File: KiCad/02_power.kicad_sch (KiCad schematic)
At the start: 51 parts, among them IC201 MCP73831T-2ACI_OT, J201 Barrel_Jack_Switch_Pin3Ring, J202 BM02B-GHS-TBT_LF__SN__N_, Q201 DMG3415U-7, U201 AMS1117-3.3, U202 TLV62569DBV

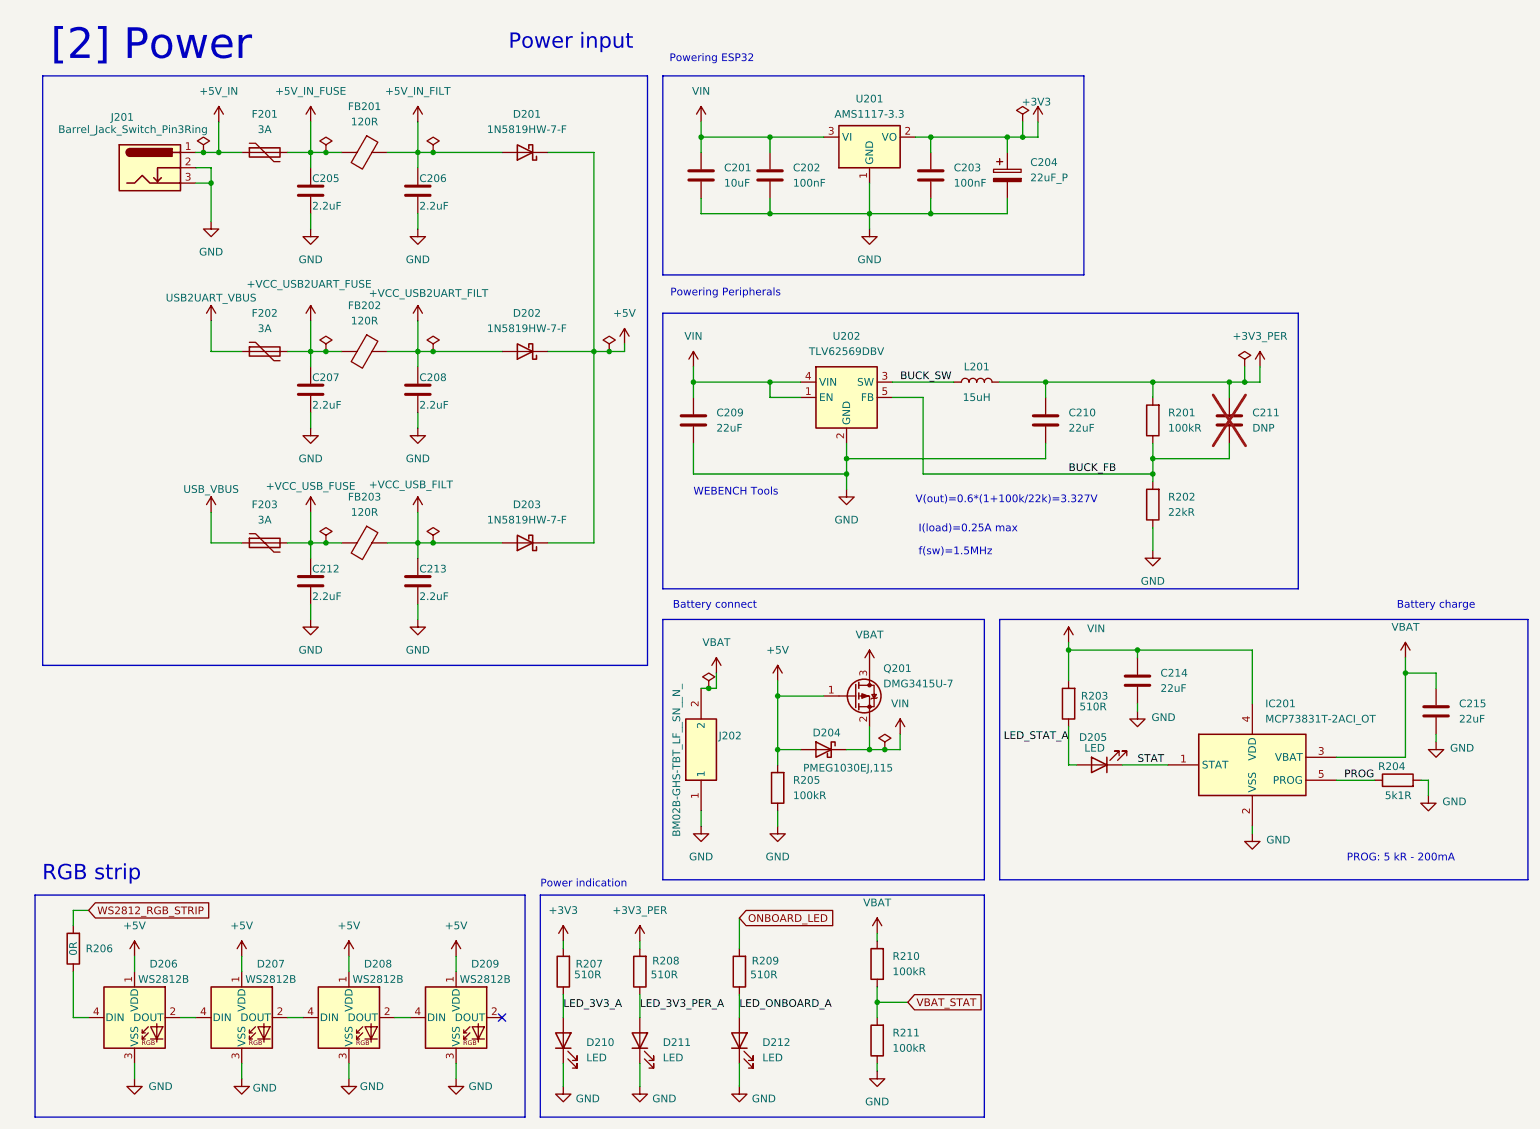
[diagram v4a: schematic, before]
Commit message: Remove broken scheme parts
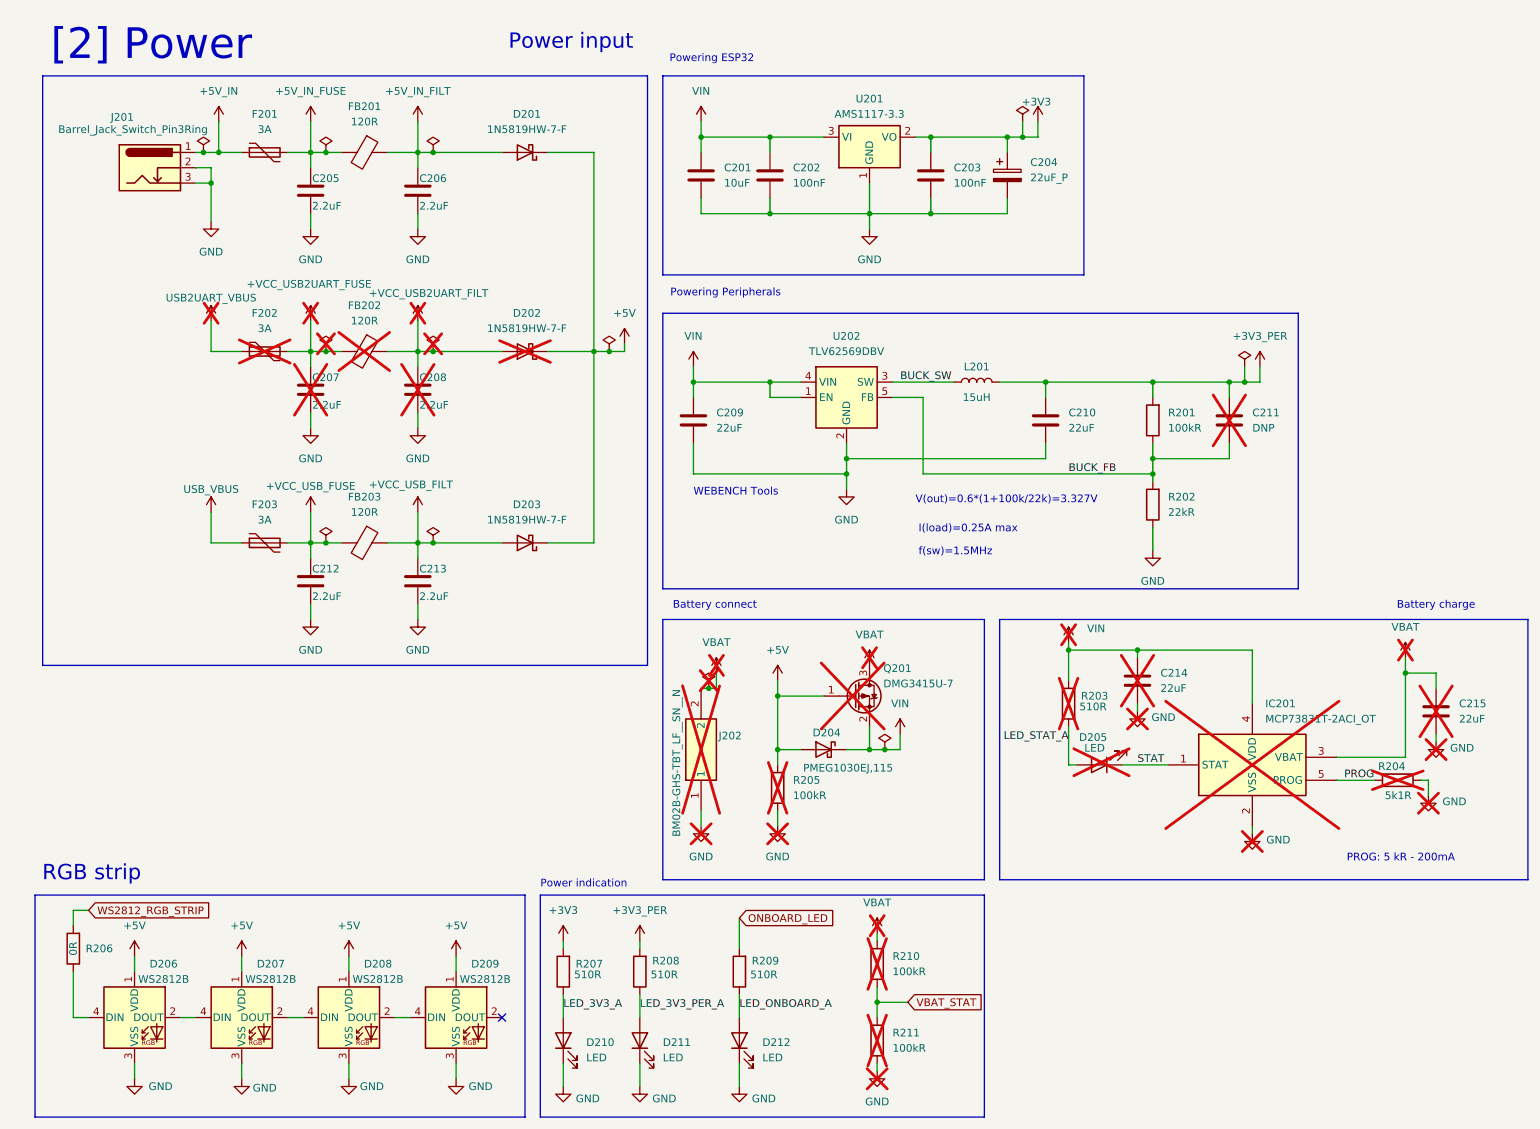
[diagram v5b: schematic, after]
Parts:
- C207, C208, C214, C215, D202, D205, F202, FB202, Q201, R203, R204, R205, R210, R211: now not fitted
- IC201: Manufacturer_Name Microchip -> (none); Manufacturer_Part_Number MCP73831T-2ACI/OT -> (none); Mouser Part Number 579-MCP73831T-2ACIOT -> (none); Mouser Price/Stock https://www.mouser.co.uk/ProductDetail/Microchip-Technology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 -> (none); now not fitted
- J202: Manufacturer_Name JST (JAPAN SOLDERLESS TERMINALS) -> (none); Manufacturer_Part_Number BM02B-GHS-TBT(LF)(SN)(N) -> (none); now not fitted
